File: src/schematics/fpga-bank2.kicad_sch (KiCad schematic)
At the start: 7 parts

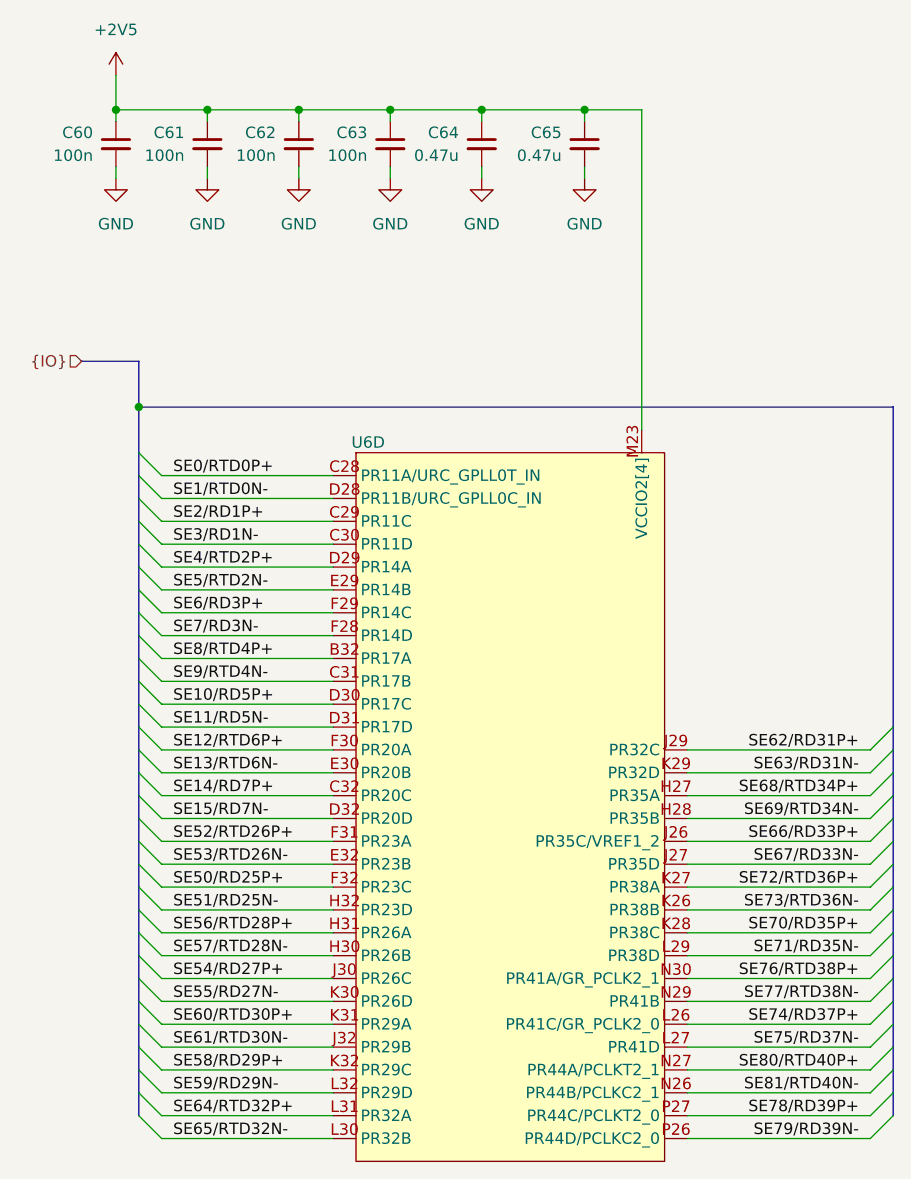
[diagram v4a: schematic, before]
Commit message: ✨ Replace some LVDS diff pairs with 3v3 single-ended signals (#56)
* ✨ Replace some LVDS diff pairs with 3v3 single-ended signals

* Finishes replacing LVDS diff pairs with 3v3 single ended
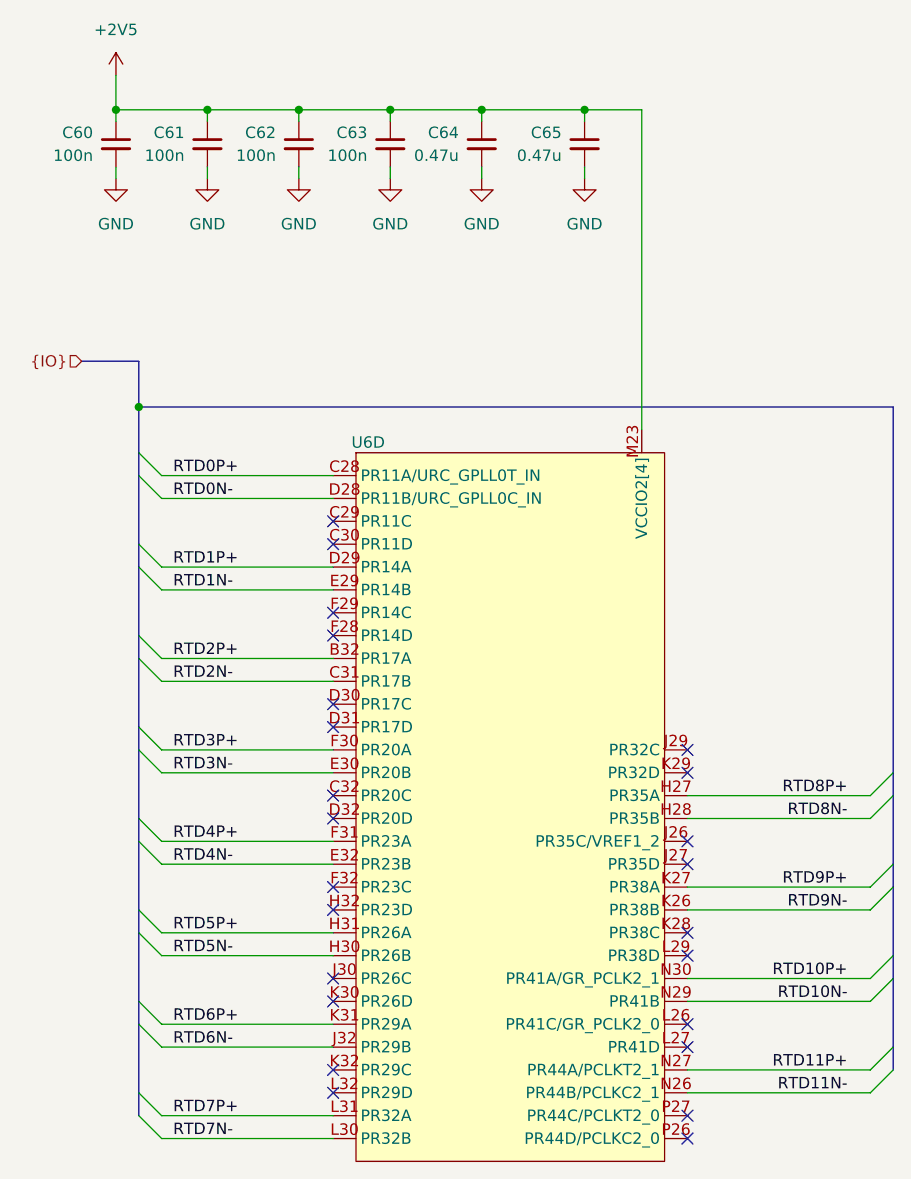
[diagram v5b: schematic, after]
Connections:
- net SE0/RTD0P+ renamed RTD0P+
- net SE10/RD5P+: no longer names the net of U6.D30 (PR17C)
- net SE11/RD5N-: no longer names the net of U6.D31 (PR17D)
- net SE12/RTD6P+ renamed RTD3P+
- net SE13/RTD6N- renamed RTD3N-
- net SE14/RD7P+: no longer names the net of U6.C32 (PR20C)
- net SE15/RD7N-: no longer names the net of U6.D32 (PR20D)
- net SE1/RTD0N- renamed RTD0N-
- net SE2/RD1P+: no longer names the net of U6.C29 (PR11C)
- net SE3/RD1N-: no longer names the net of U6.C30 (PR11D)
- net SE4/RTD2P+ renamed RTD1P+
- net SE50/RD25P+: no longer names the net of U6.F32 (PR23C)
- net SE51/RD25N-: no longer names the net of U6.H32 (PR23D)
- net SE52/RTD26P+ renamed RTD4P+
- net SE53/RTD26N- renamed RTD4N-
- net SE54/RD27P+: no longer names the net of U6.J30 (PR26C)
- net SE55/RD27N-: no longer names the net of U6.K30 (PR26D)
- net SE56/RTD28P+ renamed RTD5P+
- net SE57/RTD28N- renamed RTD5N-
- net SE58/RD29P+: no longer names the net of U6.K32 (PR29C)
- net SE59/RD29N-: no longer names the net of U6.L32 (PR29D)
- net SE5/RTD2N- renamed RTD1N-
- net SE60/RTD30P+ renamed RTD6P+
- net SE61/RTD30N- renamed RTD6N-
- net SE62/RD31P+: no longer names the net of U6.J29 (PR32C)
- net SE63/RD31N-: no longer names the net of U6.K29 (PR32D)
- net SE64/RTD32P+ renamed RTD7P+
- net SE65/RTD32N- renamed RTD7N-
- net SE66/RD33P+: no longer names the net of U6.J26 (PR35C/VREF1_2)
- net SE67/RD33N-: no longer names the net of U6.J27 (PR35D)
- net SE68/RTD34P+ renamed RTD8P+
- net SE69/RTD34N- renamed RTD8N-
- net SE6/RD3P+: no longer names the net of U6.F29 (PR14C)
- net SE70/RD35P+: no longer names the net of U6.K28 (PR38C)
- net SE71/RD35N-: no longer names the net of U6.L29 (PR38D)
- net SE72/RTD36P+ renamed RTD9P+
- net SE73/RTD36N- renamed RTD9N-
- net SE74/RD37P+: no longer names the net of U6.L26 (PR41C/GR_PCLK2_0)
- net SE75/RD37N-: no longer names the net of U6.L27 (PR41D)
- net SE76/RTD38P+ renamed RTD10P+
- net SE77/RTD38N- renamed RTD10N-
- net SE78/RD39P+: no longer names the net of U6.P27 (PR44C/PCLKT2_0)
- net SE79/RD39N-: no longer names the net of U6.P26 (PR44D/PCLKC2_0)
- net SE7/RD3N-: no longer names the net of U6.F28 (PR14D)
- net SE80/RTD40P+ renamed RTD11P+
- net SE81/RTD40N- renamed RTD11N-
- net SE8/RTD4P+ renamed RTD2P+
- net SE9/RTD4N- renamed RTD2N-
- no-connect marks 0 -> 24

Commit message: Add footprint for ecp5 (#75)
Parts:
- U6: footprint (none) -> ECAP5-DPROC:LFE5U-85F-_BG756C
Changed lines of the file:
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@@
 			)
 		)
-		(property "Footprint" ""
+		(property "Footprint" "ECAP5-DPROC:LFE5U-85F-_BG756C"
 			(at 144.78 74.93 0)
 			(effects

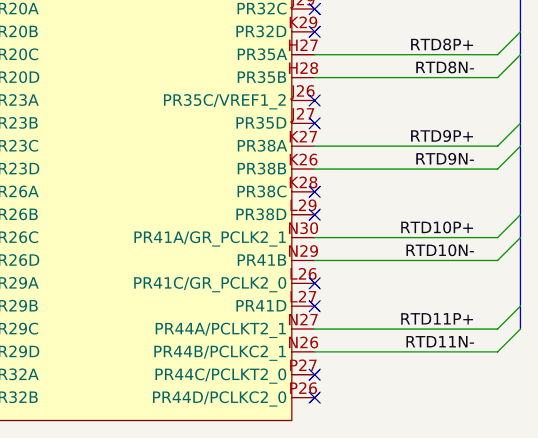
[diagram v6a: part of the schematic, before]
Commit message: Add footprint for the io connector
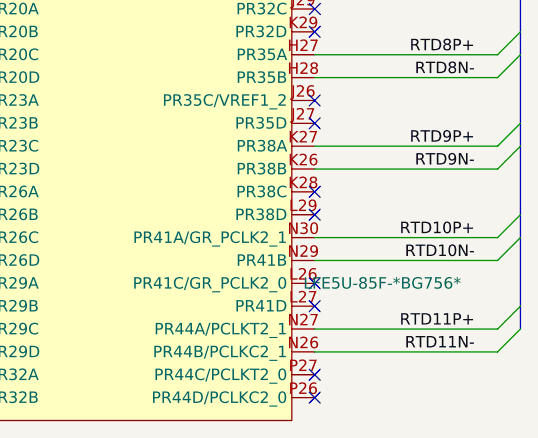
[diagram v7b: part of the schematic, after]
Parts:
- U6: value ~ -> LFE5U-85F-*BG756*
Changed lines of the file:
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@@
 			)
 		)
-		(property "Value" "~"
+		(property "Value" "LFE5U-85F-*BG756*"
 			(at 177.8 135.89 0)
 			(effects

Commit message: Add remaining component footprints (#79)
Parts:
- C60, C61, C62, C63, C64, C65: footprint (none) -> Capacitor_SMD:C_0402_1005Metric
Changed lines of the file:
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@@
 			)
 		)
-		(property "Footprint" ""
+		(property "Footprint" "Capacitor_SMD:C_0402_1005Metric"
 			(at 115.57 38.1 0)
 			(effects
@@
 			)
 		)
-		(property "Footprint" ""
+		(property "Footprint" "Capacitor_SMD:C_0402_1005Metric"
 			(at 135.89 38.1 0)
 			(effects
@@
 			)
 		)
-		(property "Footprint" ""
+		(property "Footprint" "Capacitor_SMD:C_0402_1005Metric"
 			(at 167.64 38.1 0)
 			(effects
@@
 			)
 		)
-		(property "Footprint" ""
+		(property "Footprint" "Capacitor_SMD:C_0402_1005Metric"
 			(at 156.21 38.1 0)
 			(effects
@@
 			)
 		)
-		(property "Footprint" ""
+		(property "Footprint" "Capacitor_SMD:C_0402_1005Metric"
 			(at 125.73 38.1 0)
 			(effects
@@
 			)
 		)
-		(property "Footprint" ""
+		(property "Footprint" "Capacitor_SMD:C_0402_1005Metric"
 			(at 146.05 38.1 0)
 			(effects
